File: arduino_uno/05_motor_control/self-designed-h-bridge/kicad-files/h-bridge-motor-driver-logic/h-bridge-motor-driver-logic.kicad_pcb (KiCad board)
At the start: 2 copper layers, 2 parts, among them J1 Conn_01x05_Pin, J2 Conn_01x03_Pin

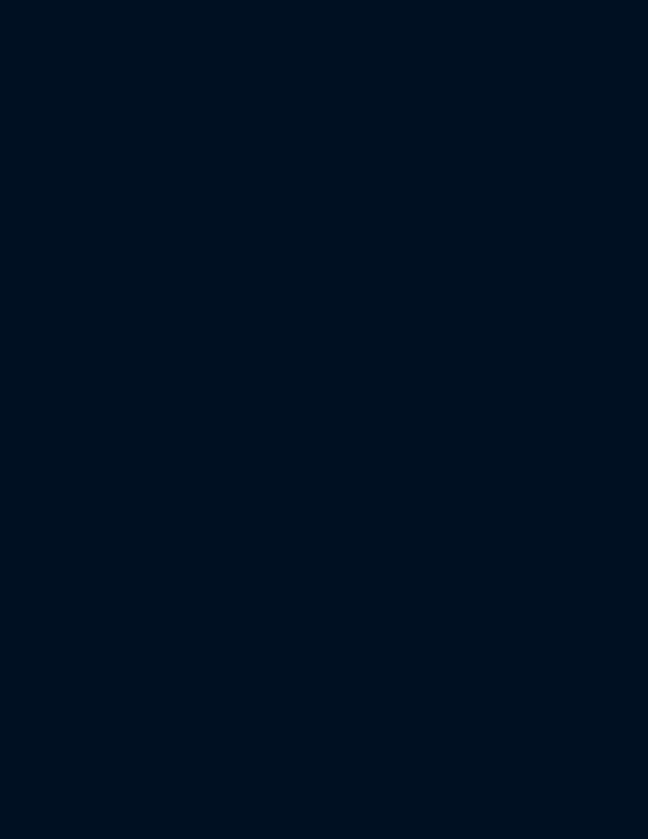
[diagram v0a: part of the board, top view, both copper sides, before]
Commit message: add labels to connector
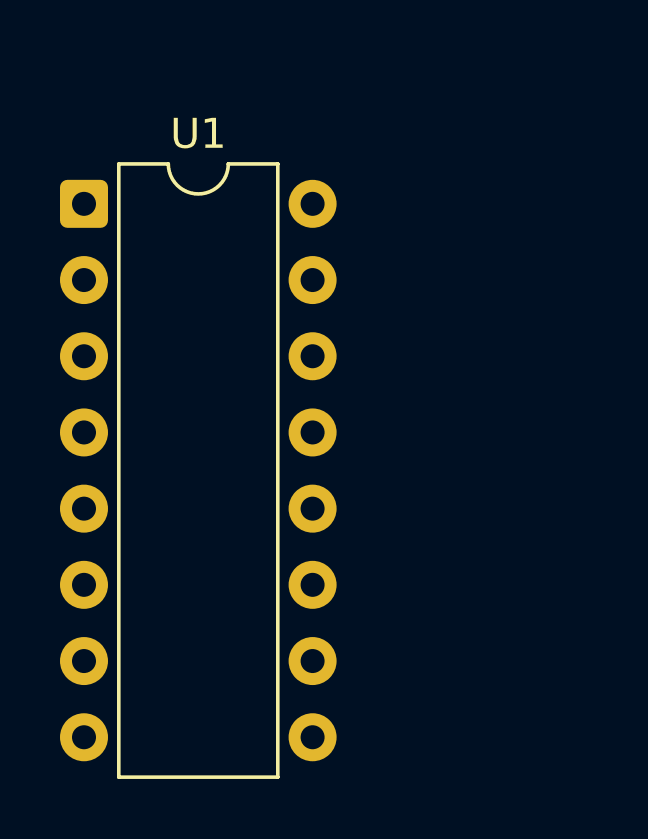
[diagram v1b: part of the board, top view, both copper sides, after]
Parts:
- added U1: PC847, Package_DIP:DIP-16_W7.62mm, F.Cu at (65.9, 72.7)
